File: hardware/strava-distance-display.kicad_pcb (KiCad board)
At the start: 2 copper layers, 50.8 x 27.9 mm, 17 parts, among them J1 Display, J2 Battery, J3 FTDI_CONN, SW1 reset, SW2 prog enable, U1 ESP-12F, U2 LD1117S33TR_SOT223

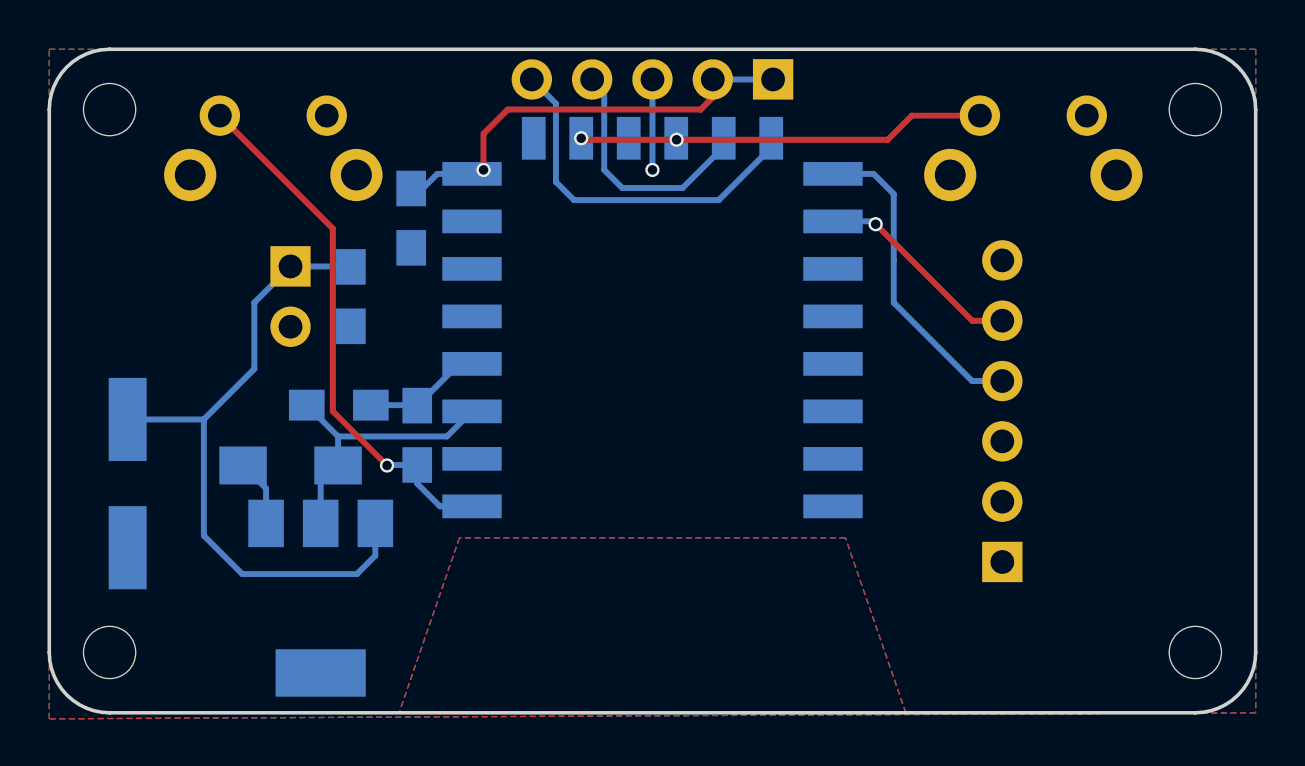
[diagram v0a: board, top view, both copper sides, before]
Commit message: Schematic now uses built-in KiCad's ESP-12F symbol + footprint.
And all the related error fixes as well..
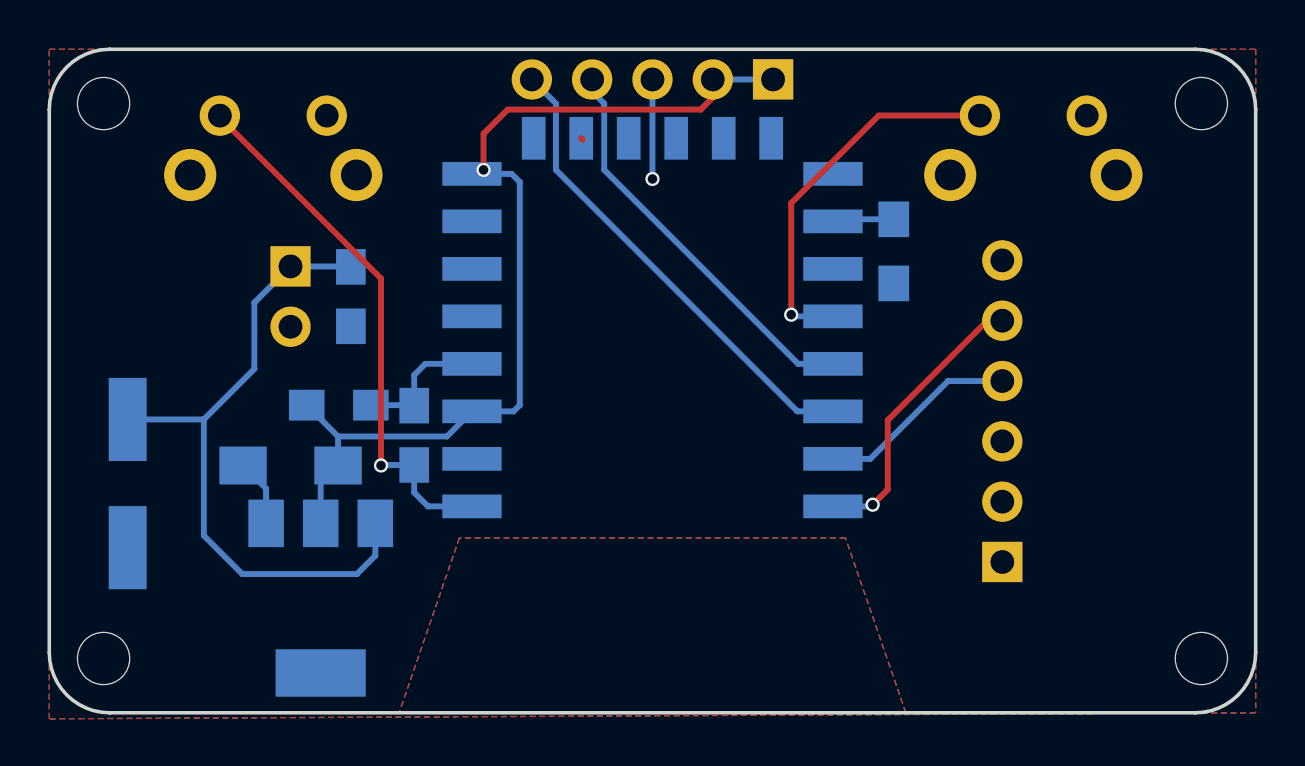
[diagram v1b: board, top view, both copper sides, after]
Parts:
- removed C3: 100nF, Capacitors_SMD:C_0805_HandSoldering
- added R2: 10K, Resistors_SMD:R_0805_HandSoldering, B.Cu at (157.5, 95.6)
- U1: value ESP-12F -> ESP-12E
- moved REF** 0.36 mm to (170.4, 89.4)
- moved REF** 0.36 mm to (124.2, 89.4)
- moved REF** 0.36 mm to (124.2, 112.8)
- moved REF** 0.36 mm to (170.4, 112.8)
- moved C2 0.13 mm to (137.3, 103.4), turned to 270 degrees
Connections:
- R1 pad 1: Net-(C2-Pad2) -> Net-(C2-Pad1)
- SW1 pad 2: Net-(C2-Pad1) -> Net-(C2-Pad2)
- U1 pad 1: Net-(C2-Pad1) -> Net-(C2-Pad2)
- U1 pad 10: Net-(SW2-Pad2) -> (no net)
- U1 pad 12: Net-(SW2-Pad2) -> (no net)
- U1 pad 13: Net-(J1-Pad4) -> (no net)
- U1 pad 14: Net-(J1-Pad5) -> (no net)
- U1 pad 15: Net-(J3-Pad4) -> GND
- U1 pad 16: Net-(J3-Pad5) -> Net-(R2-Pad1)
- U1 pad 18: (no net) -> Net-(SW2-Pad2)
- U1 pad 19: (no net) -> Net-(J1-Pad4)
- U1 pad 20: (no net) -> Net-(J1-Pad5)
- U1 pad 21: (no net) -> Net-(J3-Pad4)
- U1 pad 22: (no net) -> Net-(J3-Pad5)
- U1 pad 4: Net-(C2-Pad2) -> Net-(C2-Pad1)
- U1 pad 9: GND -> (no net)
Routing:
- net Net-(C2-Pad2): track 4.99 -> 22.8 mm, vias 0 -> 1
- net Net-(C2-Pad1): track 22.9 -> 6.24 mm, vias 1 -> 0
- net +3V3: track 31.2 -> 42.0 mm
- net Net-(J1-Pad4): track 10.4 -> 17.0 mm
- net Net-(J3-Pad4): track 14.2 -> 8.49 mm
- net Net-(J1-Pad5): track 15.4 -> 20.1 mm
- net Net-(J3-Pad5): track 8.86 -> 12.1 mm
- net Net-(R2-Pad1): track 0.00 -> 2.60 mm
- net Net-(SW2-Pad2): track 17.3 -> 16.0 mm, vias 2 -> 1
